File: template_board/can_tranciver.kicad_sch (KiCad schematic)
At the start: 6 parts, among them SW2 SW_DIP_x01, U2 TJA1044GTK_3Z

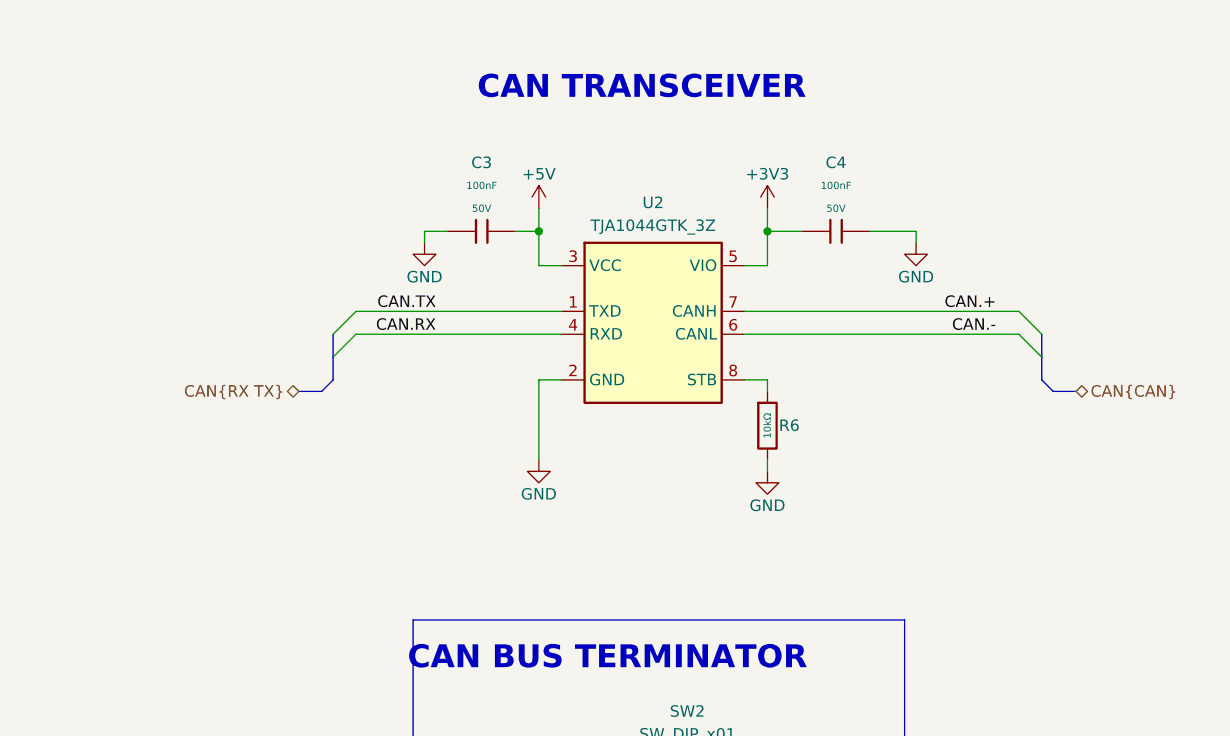
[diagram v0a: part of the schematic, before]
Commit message: added can fb transiver
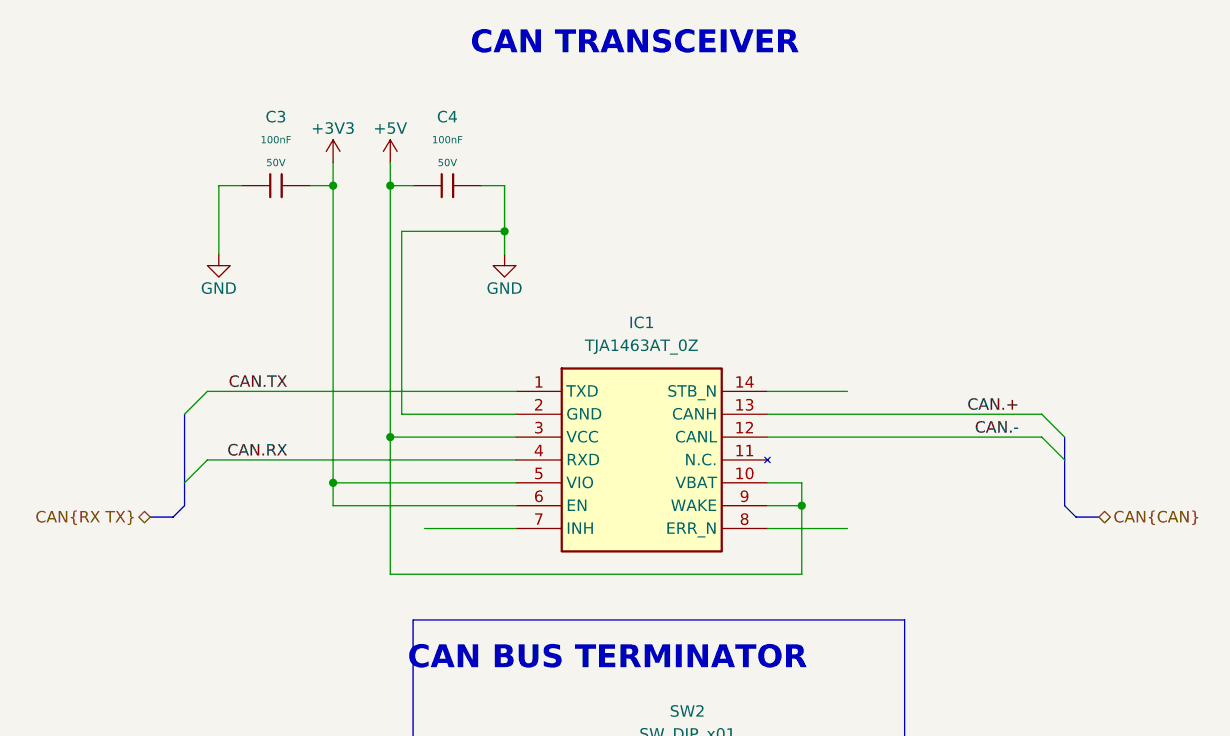
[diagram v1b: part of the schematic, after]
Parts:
- removed R6: 10kΩ, PCM_JLCPCB:R_0402, symbol PCM_JLCPCB-Resistors:0402,10kΩ
- removed U2: TJA1044GTK_3Z, Package_SON:HVSON-8-1EP_3x3mm_P0.65mm_EP1.6x2.4mm, symbol TJA1044GTK_3Z:TJA1044GTK_3Z
- added IC1: TJA1463AT_0Z, SOIC127P600X175-14N, symbol TJA1463AT_0Z:TJA1463AT_0Z
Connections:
- net +3V3: now also C3.2, IC1.5 (VIO), IC1.6 (EN); no longer C4.1
- net +5V: now also C4.1, IC1.10 (VBAT), IC1.3 (VCC), IC1.9 (WAKE); no longer C3.2
- net CAN.+: now also IC1.13 (CANH)
- net CAN.-: now also IC1.12 (CANL)
- net CAN.RX: now also IC1.4 (RXD)
- net CAN.TX: now also IC1.1 (TXD)
- net GND: now also IC1.2 (GND)

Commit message: can transiver update
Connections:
- net POWER_EN: now reaches IC1.7 (INH)
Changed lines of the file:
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@@
 	)
 	(bus_entry
-		(at 194.31 106.68)
+		(at 176.53 106.68)
 		(size -2.54 -2.54)
 		(stroke
@@
 	)
 	(bus_entry
-		(at 191.77 101.6)
+		(at 173.99 101.6)
 		(size 2.54 2.54)
 		(stroke
@@
 	(bus
 		(pts
-			(xy 194.31 111.76) (xy 195.58 113.03)
+			(xy 176.53 111.76) (xy 177.8 113.03)
 		)
 		(stroke
@@
 	(wire
 		(pts
+			(xy 113.03 114.3) (xy 133.35 114.3)
+		)
+		(stroke
+			(width 0)
+			(type default)
+		)
+	)
+	(wire
+		(pts
 			(xy 110.49 76.2) (xy 113.03 76.2)
 		)
@@
 	(wire
 		(pts
-			(xy 123.19 114.3) (xy 133.35 114.3)
-		)
-		(stroke
-			(width 0)
-			(type default)
-		)
-	)
-	(wire
-		(pts
 			(xy 132.08 81.28) (xy 132.08 83.82)
 		)
@@
 	(wire
 		(pts
-			(xy 161.29 99.06) (xy 170.18 99.06)
+			(xy 161.29 99.06) (xy 193.04 99.06)
 		)
 		(stroke
@@
 	(wire
 		(pts
-			(xy 161.29 114.3) (xy 170.18 114.3)
+			(xy 161.29 114.3) (xy 193.04 114.3)
 		)
 		(stroke
@@
 	(wire
 		(pts
-			(xy 120.65 101.6) (xy 120.65 81.28)
+			(xy 128.27 101.6) (xy 128.27 81.28)
 		)
 		(stroke
@@
 	(wire
 		(pts
-			(xy 161.29 104.14) (xy 191.77 104.14)
-		)
-		(stroke
-			(width 0)
-			(type default)
-		)
-	)
-	(wire
-		(pts
-			(xy 120.65 81.28) (xy 132.08 81.28)
+			(xy 161.29 104.14) (xy 173.99 104.14)
+		)
+		(stroke
+			(width 0)
+			(type default)
+		)
+	)
+	(wire
+		(pts
+			(xy 128.27 81.28) (xy 132.08 81.28)
 		)
 		(stroke
@@
 	(bus
 		(pts
-			(xy 194.31 106.68) (xy 194.31 111.76)
+			(xy 176.53 106.68) (xy 176.53 111.76)
 		)
 		(stroke
@@
 	(wire
 		(pts
-			(xy 133.35 101.6) (xy 120.65 101.6)
+			(xy 133.35 101.6) (xy 128.27 101.6)
 		)
 		(stroke
@@
 	(wire
 		(pts
-			(xy 161.29 101.6) (xy 191.77 101.6)
+			(xy 161.29 101.6) (xy 173.99 101.6)
 		)
 		(stroke
@@
 	(bus
 		(pts
-			(xy 194.31 104.14) (xy 194.31 106.68)
+			(xy 176.53 104.14) (xy 176.53 106.68)
 		)
 		(stroke
@@
 	(bus
 		(pts
-			(xy 195.58 113.03) (xy 198.12 113.03)
+			(xy 177.8 113.03) (xy 180.34 113.03)
 		)
 		(stroke
@@
 	)
 	(label "CAN.-"
-		(at 189.23 104.14 180)
+		(at 171.45 104.14 180)
 		(effects
 			(font
@@
 	)
 	(label "CAN.+"
-		(at 189.23 101.6 180)
+		(at 171.45 101.6 180)
 		(effects
 			(font
@@
 			)
 			(justify right bottom)
+		)
+	)
+	(hierarchical_label "POWER_EN"
+		(shape output)
+		(at 113.03 114.3 180)
+		(effects
+			(font
+				(size 1.27 1.27)
+			)
+			(justify right)
 		)
 	)
@@
 	(hierarchical_label "CAN{CAN}"
 		(shape bidirectional)
-		(at 198.12 113.03 0)
-		(effects
-			(font
+		(at 180.34 113.03 0)
+		(effects
+			(font

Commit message: chamt skończony chyba
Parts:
- removed C3, C4: 100nF, PCM_JLCPCB:C_0402, symbol PCM_JLCPCB-Capacitors:0402,100nF,(2)
- removed IC1: TJA1463AT_0Z, SOIC127P600X175-14N, symbol TJA1463AT_0Z:TJA1463AT_0Z
- added C17, C18: 100nF, PCM_JLCPCB:C_0402, symbol PCM_JLCPCB-Capacitors:0402,100nF,(2)
- added C3: 100nF, PCM_JLCPCB:C_0402, symbol PCM_JLCPCB-Capacitors:0402,100nF
- added R12, R13: 10kΩ, PCM_JLCPCB:R_0402, symbol PCM_JLCPCB-Resistors:0402,10kΩ
- added SW3: SW_Push, lib:TS1088R02026, symbol Switch:SW_Push
- added U6: TJA1145T, Package_SO:SOIC-14_3.9x8.7mm_P1.27mm, symbol Interface_CAN_LIN:TJA1145T
- SW2: footprint (none) -> Button_Switch_THT:SW_DIP_SPSTx01_Slide_9.78x4.72mm_W7.62mm_P2.54mm
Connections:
- net +3V3: now also C18.2, R13.1, SW3.2, U6.5 (VIO)
- net CAN.+: now also U6.13 (CANH)
- net CAN.-: now also U6.12 (CANL)
- net CAN.RX: now also U6.1 (TXD)
- net CAN.TX: now also U6.4 (RXD)
- net GND: now also C17.1, C18.1, C3.2, R12.2, U6.2 (GND)
- net POWER_EN: now also U6.7 (INH)
- new net +5V_unprotected: C17.2, U6.10 (BAT), U6.3 (VCC)
- new net CAN_TRANSIVER.CLK: U6.8 (SCK)
- new net CAN_TRANSIVER.CS: U6.14 (~{SCS})
- new net CAN_TRANSIVER.MISO: U6.6 (SDO)
- new net CAN_TRANSIVER.MOSI: U6.11 (SDI)
- new net WAKE: C3.1, R12.1, R13.2, SW3.1, U6.9 (WAKE)
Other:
- note added: "WAKE BUTTON"
- moved on the sheet: R2, SW2

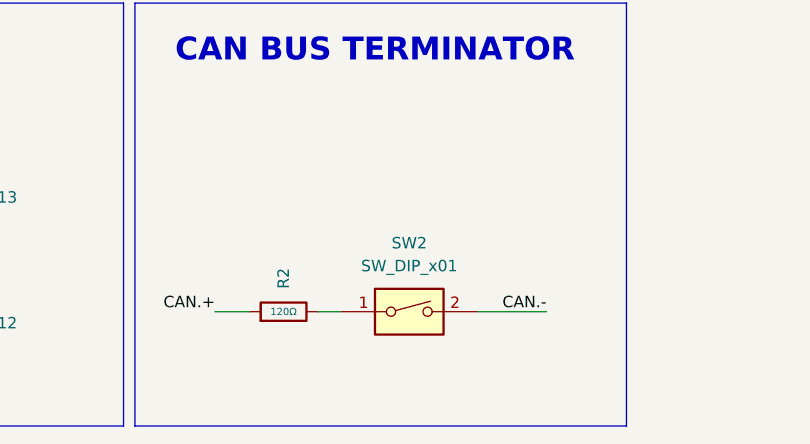
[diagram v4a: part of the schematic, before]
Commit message: fixed USB\Power leyout , added proper RF rules adn paths
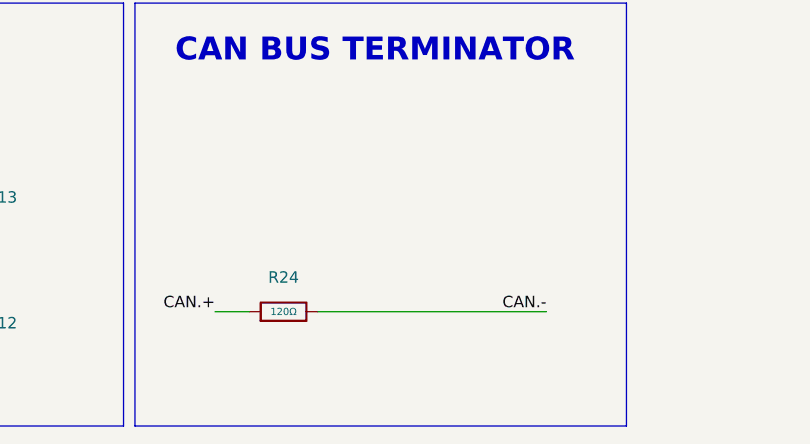
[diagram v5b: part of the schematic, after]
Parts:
- removed R2: 120Ω, PCM_JLCPCB:R_0402, symbol PCM_JLCPCB-Resistors:0402,120Ω
- removed SW2: SW_DIP_x01, Button_Switch_THT:SW_DIP_SPSTx01_Slide_9.78x4.72mm_W7.62mm_P2.54mm, symbol Switch:SW_DIP_x01
- added R24: 120Ω, PCM_JLCPCB:R_0603, symbol PCM_JLCPCB-Resistors:0603,120Ω
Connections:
- net CAN.+: now also R24.1
- net CAN.-: now also R24.2
